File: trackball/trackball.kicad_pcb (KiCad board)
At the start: 2 copper layers, 15 x 13.4 mm, 8 parts, among them P8 CONN_7, U1 TLE4964-5M, U2 TLE4964-5M, U3 TLE4964-5M, U4 TLE4964-5M

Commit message: Bump version number to 1.2.0
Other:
- board text added: "v1.2.0"
- board text removed: "v1.1.0"
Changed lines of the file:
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@@
-(kicad_pcb (version 20171130) (host pcbnew "(5.1.5)-2")
+(kicad_pcb (version 20171130) (host pcbnew 5.1.5-52549c5~84~ubuntu18.04.1)
   (general
     (thickness 1.6)
@@
   (title_block
     (title "UHK Key Cluster Module - Trackball Board")
-    (rev 1.1.0)
+    (rev 1.2.0)
     (company "Ultimate Gadget Laboratories Kft.")
   )
@@
   )
   (setup
-    (last_trace_width 0.381)
+    (last_trace_width 0.2032)
     (user_trace_width 0.2032)
     (user_trace_width 0.254)
@@
   (gr_arc (start 205.382248 150.782505) (end 204.420921 150.506909) (angle -90) (layer Edge.Cuts) (width 0.01))
   (gr_arc (start 200.187782 143.931454) (end 200.937782 143.931454) (angle -180) (layer Edge.Cuts) (width 0.01))
-  (gr_text v1.1.0 (at 196.6 145 17) (layer B.SilkS)
+  (gr_text v1.2.0 (at 196.6 145 17) (layer B.SilkS)
     (effects (font (size 0.75 0.75) (thickness 0.15)) (justify mirror))
   )
@@
   (segment (start 198.5 149.1) (end 198.5 149.9) (width 0.254) (layer B.Cu) (net 1))
   (via (at 198.45 153.95) (size 0.7112) (drill 0.381) (layers F.Cu B.Cu) (net 1))
-  (segment (start 200.390425 147.2438) (end 200.335876 147.189251) (width 0.254) (layer F.Cu) (net 2))
-  (segment (start 200.085625 146.939) (end 200.335876 147.189251) (width 0.254) (layer F.Cu) (net 2))
-  (segment (start 199.9996 146.939) (end 200.085625 146.939) (width 0.254) (layer F.Cu) (net 2))
   (segment (start 203.4 155.03982) (end 203.58982 154.85) (width 0.254) (layer F.Cu) (net 1))
   (via (at 204.35 154.85) (size 0.7112) (drill 0.381) (layers F.Cu B.Cu) (net 1))
@@
   (via (at 198.6026 151.3078) (size 0.7112) (drill 0.381) (layers F.Cu B.Cu) (net 1))
   (segment (start 198.6026 150.2664) (end 197.485 149.1488) (width 0.508) (layer B.Cu) (net 1))
+  (segment (start 200.390425 147.2438) (end 200.335876 147.189251) (width 0.254) (layer F.Cu) (net 2))
+  (segment (start 200.085625 146.939) (end 200.335876 147.189251) (width 0.254) (layer F.Cu) (net 2))
+  (segment (start 199.9996 146.939) (end 200.085625 146.939) (width 0.254) (layer F.Cu) (net 2))
   (segment (start 199 146.999237) (end 199 149.1) (width 0.254) (layer B.Cu) (net 2))
   (via (at 199.009 147.193) (size 0.7112) (drill 0.381) (layers F.Cu B.Cu) (net 2))

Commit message: Bump the version number of both boards to 2.0.0
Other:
- board text added: "v2.0.0"
- board text removed: "v1.2.0"
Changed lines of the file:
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@@
   (title_block
     (title "UHK Key Cluster Module - Trackball Board")
-    (rev 1.2.0)
+    (rev 2.0.0)
     (company "Ultimate Gadget Laboratories Kft.")
   )
@@
   (gr_arc (start 205.382248 150.782505) (end 204.420921 150.506909) (angle -90) (layer Edge.Cuts) (width 0.01))
   (gr_arc (start 200.187782 143.931454) (end 200.937782 143.931454) (angle -180) (layer Edge.Cuts) (width 0.01))
-  (gr_text v1.2.0 (at 196.6 145 17) (layer B.SilkS)
+  (gr_text v2.0.0 (at 196.6 145 17) (layer B.SilkS)
     (effects (font (size 0.75 0.75) (thickness 0.15)) (justify mirror))
   )

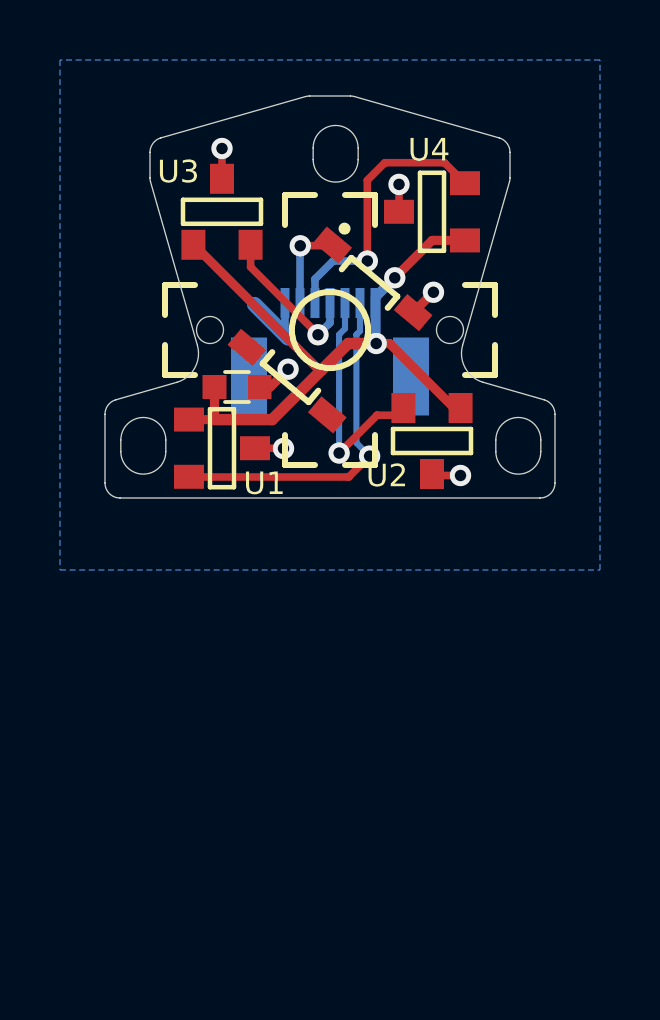
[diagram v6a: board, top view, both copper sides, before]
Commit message: Remove unneeded capacitor.
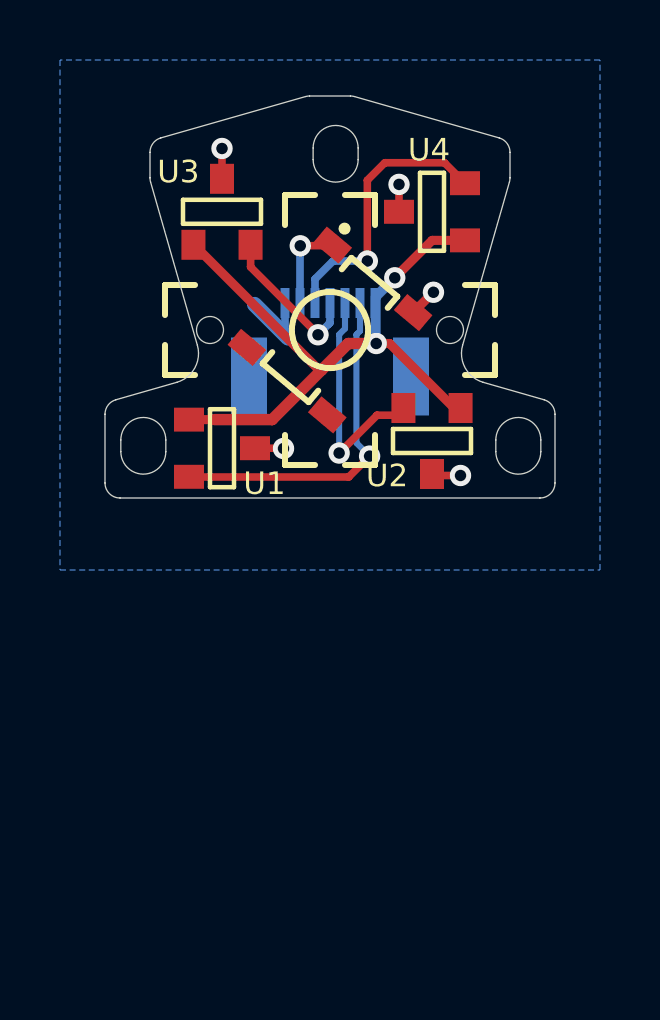
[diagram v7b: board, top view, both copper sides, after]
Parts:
- removed C1: 0.1uF, UGL:SM0603
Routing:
- net GND: track 8.44 -> 7.25 mm, vias 6 -> 5
- net +3V3: track 23.6 -> 22.5 mm
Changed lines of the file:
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@@
     (thickness 1.6)
     (drawings 41)
-    (tracks 75)
+    (tracks 71)
     (zones 0)
-    (modules 8)
+    (modules 7)
     (nets 8)
   )
@@
     (visible_elements 7FFFFF7F)
     (pcbplotparams
-      (layerselection 0x00030_ffffffff)
+      (layerselection 0x010fc_ffffffff)
       (usegerberextensions true)
       (usegerberattributes false)
@@
       (outputformat 1)
       (mirror false)
-      (drillshape 1)
+      (drillshape 0)
       (scaleselection 1)
       (outputdirectory ""))
@@
     (pad "" np_thru_hole circle (at 4 0) (size 0.9 0.9) (drill 0.9) (layers *.Cu *.Mask))
     (pad "" np_thru_hole circle (at -4 0) (size 0.9 0.9) (drill 0.9) (layers *.Cu *.Mask))
-  )
-  (module UGL:SM0603 (layer F.Cu)
-    (at 196.9 151.9 180)
-    (attr smd)
-    (fp_text reference C1 (at 1.5 -0.9 180) (layer B.SilkS)
-      (effects (font (size 0.75 0.75) (thickness 0.15)) (justify mirror))
-    )
-    (fp_text value 0.1uF (at 0.6 -2 180) (layer B.SilkS)
-      (effects (font (size 0.75 0.75) (thickness 0.15)) (justify mirror))
-    )
-    (fp_line (start -0.4 -0.5) (end 0.4 -0.5) (layer F.SilkS) (width 0.127))
-    (fp_line (start 0.4 0.5) (end -0.4 0.5) (layer F.SilkS) (width 0.127))
-    (pad 1 smd rect (at -0.75 0 180) (size 0.8 0.8) (layers F.Cu F.Paste F.Mask)
-      (net 1 GND))
-    (pad 2 smd rect (at 0.75 0 180) (size 0.8 0.8) (layers F.Cu F.Paste F.Mask)
-      (net 4 +3V3))
-    (model smd\resistors\R0603.wrl
-      (offset (xyz 0 0 0.02540000082496551))
-      (scale (xyz 0.5 0.5 0.5))
-      (rotate (xyz 0 0 0))
-    )
   )
   (module UGL:TL3315NF250Q (layer F.Cu)
@@
   (segment (start 202.770779 149.420429) (end 203.448808 148.7424) (width 0.3048) (layer F.Cu) (net 1))
   (via (at 203.448808 148.7424) (size 0.7112) (drill 0.381) (layers F.Cu B.Cu) (net 1))
-  (segment (start 198.0104 151.9) (end 198.6026 151.3078) (width 0.3048) (layer F.Cu) (net 1))
-  (segment (start 197.65 151.9) (end 198.0104 151.9) (width 0.3048) (layer F.Cu) (net 1))
-  (via (at 198.6026 151.3078) (size 0.7112) (drill 0.381) (layers F.Cu B.Cu) (net 1))
   (segment (start 198.6026 150.2664) (end 197.485 149.1488) (width 0.508) (layer B.Cu) (net 1))
   (segment (start 200.390425 147.2438) (end 200.335876 147.189251) (width 0.254) (layer F.Cu) (net 2))
@@
   (segment (start 201.9866 150.45) (end 201.541198 150.45) (width 0.3048) (layer F.Cu) (net 4))
   (segment (start 204.3525 152.8159) (end 201.9866 150.45) (width 0.3048) (layer F.Cu) (net 4))
-  (segment (start 196.15 152.9875) (end 196.15 151.9) (width 0.3048) (layer F.Cu) (net 4))
   (segment (start 195.30018 152.9875) (end 196.15 152.9875) (width 0.3048) (layer F.Cu) (net 4))
   (segment (start 200.608662 150.45) (end 201.541198 150.45) (width 0.381) (layer F.Cu) (net 4))

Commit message: Update contour to rigid-flex.
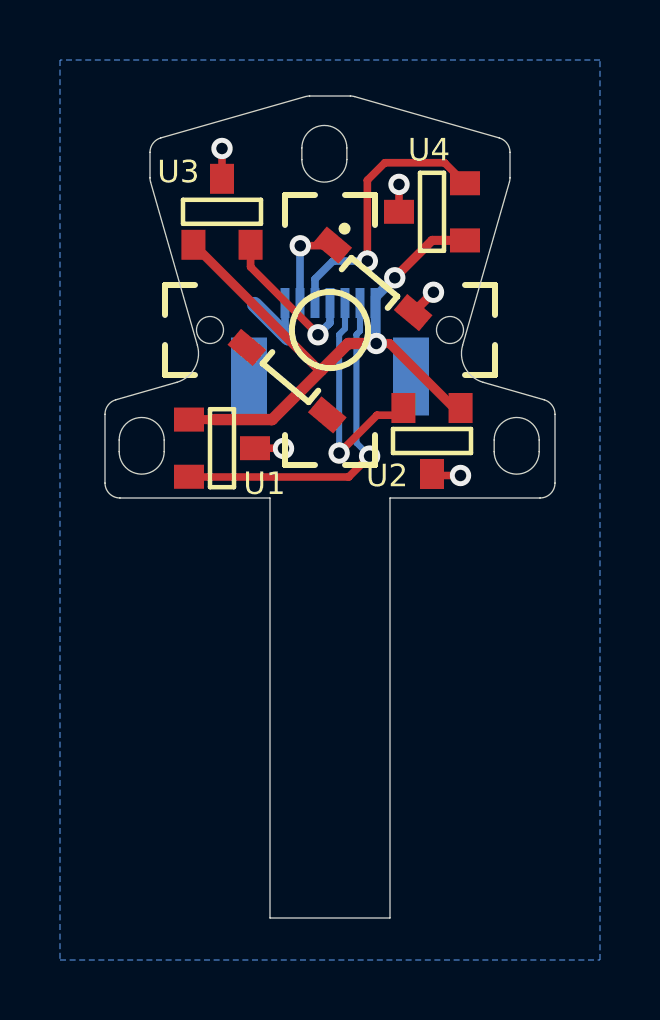
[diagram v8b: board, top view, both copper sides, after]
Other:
- board size 15 x 13.4 mm -> 15 x 27.4 mm
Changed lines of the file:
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@@
   (general
     (thickness 1.6)
-    (drawings 41)
+    (drawings 46)
     (tracks 71)
     (zones 0)
@@
     (37 F.SilkS user)
     (38 B.Mask user)
-    (39 F.Mask user)
+    (39 F.Mask user hide)
     (40 Dwgs.User user)
     (41 Cmts.User user)
@@
     (pad_to_mask_clearance 0)
     (aux_axis_origin 0 0)
-    (visible_elements 7FFFFF7F)
+    (visible_elements 7FFFEF7F)
     (pcbplotparams
       (layerselection 0x010fc_ffffffff)
@@
     (pad 4 smd rect (at -2.225 -1.749999 230) (size 0.7 1.1) (layers F.Cu F.Paste F.Mask))
   )
+  (gr_line (start 202 155.6) (end 207 155.6) (angle 90) (layer Edge.Cuts) (width 0.01))
   (gr_circle (center 196.3 153.94) (end 196.35 153.94) (layer Eco2.User) (width 0.1))
   (gr_circle (center 203.94 146.06) (end 203.99 146.06) (layer Eco2.User) (width 0.1))
   (gr_circle (center 203.94 153.94) (end 203.99 153.94) (layer Eco2.User) (width 0.1))
   (gr_circle (center 196.06 146.06) (end 196.11 146.06) (layer Eco2.User) (width 0.1))
-  (gr_arc (start 199.320057 142.700091) (end 199.32003 142.199997) (angle -15.6) (layer Edge.Cuts) (width 0.01))
-  (gr_arc (start 200.679943 142.700091) (end 200.817329 142.219238) (angle -15.7) (layer Edge.Cuts) (width 0.01))
-  (gr_arc (start 193.000061 155.099935) (end 192.5 155.100003) (angle -89.9) (layer Edge.Cuts) (width 0.01))
-  (gr_arc (start 194.500041 144.077192) (end 194.36264 143.59639) (angle -74) (layer Edge.Cuts) (width 0.01))
-  (gr_arc (start 205.499959 144.077192) (end 206 144.077148) (angle -74) (layer Edge.Cuts) (width 0.01))
-  (gr_arc (start 206.999958 152.806915) (end 207.5 152.806897) (angle -74) (layer Edge.Cuts) (width 0.01))
-  (gr_arc (start 206.999932 155.099935) (end 207 155.600003) (angle -89.9) (layer Edge.Cuts) (width 0.01))
-  (gr_arc (start 193.000042 152.806915) (end 192.862183 152.32626) (angle -74) (layer Edge.Cuts) (width 0.01))
-  (gr_arc (start 194.5001 144.929701) (end 194 144.92973) (angle -15.97224935) (layer Edge.Cuts) (width 0.01))
-  (gr_arc (start 205.4999 144.929701) (end 205.980629 145.067548) (angle -16) (layer Edge.Cuts) (width 0.01))
-  (gr_line (start 207 155.600003) (end 193 155.600003) (angle 90) (layer Edge.Cuts) (width 0.01))
-  (gr_line (start 207.5 152.806897) (end 207.5 155.100003) (angle 90) (layer Edge.Cuts) (width 0.01))
-  (gr_line (start 192.862183 152.32626) (end 194.893456 151.743802) (angle 90) (layer Edge.Cuts) (width 0.01))
-  (gr_line (start 195.579079 150.506909) (end 194.019371 145.067548) (angle 90) (layer Edge.Cuts) (width 0.01))
-  (gr_line (start 200.817329 142.219238) (end 205.63736 143.59639) (angle 90) (layer Edge.Cuts) (width 0.01))
-  (gr_line (start 194.36264 143.59639) (end 199.182671 142.219238) (angle 90) (layer Edge.Cuts) (width 0.01))
-  (gr_line (start 194 144.92973) (end 194 144.077148) (angle 90) (layer Edge.Cuts) (width 0.01))
-  (gr_line (start 205.106544 151.743802) (end 207.137817 152.32626) (angle 90) (layer Edge.Cuts) (width 0.01))
-  (gr_line (start 199.32003 142.199997) (end 200.67997 142.199997) (angle 90) (layer Edge.Cuts) (width 0.01))
-  (gr_line (start 206 144.077148) (end 206 144.92973) (angle 90) (layer Edge.Cuts) (width 0.01))
-  (gr_line (start 205.980629 145.067548) (end 204.420921 150.506909) (angle 90) (layer Edge.Cuts) (width 0.01))
-  (gr_line (start 205.52729 154.054501) (end 205.52729 153.665707) (angle 90) (layer Edge.Cuts) (width 0.01))
-  (gr_arc (start 200.187782 144.320233) (end 199.437782 144.320233) (angle -180) (layer Edge.Cuts) (width 0.01))
-  (gr_arc (start 193.77729 153.665707) (end 194.52729 153.665707) (angle -180) (layer Edge.Cuts) (width 0.01))
-  (gr_line (start 192.5 155.100003) (end 192.5 152.806897) (angle 90) (layer Edge.Cuts) (width 0.01))
-  (gr_line (start 194.52729 153.665707) (end 194.52729 154.054501) (angle 90) (layer Edge.Cuts) (width 0.01))
-  (gr_arc (start 206.27729 153.665707) (end 207.02729 153.665707) (angle -180) (layer Edge.Cuts) (width 0.01))
-  (gr_line (start 193.02729 154.054501) (end 193.02729 153.665707) (angle 90) (layer Edge.Cuts) (width 0.01))
-  (gr_line (start 207.02729 153.665707) (end 207.02729 154.054501) (angle 90) (layer Edge.Cuts) (width 0.01))
-  (gr_arc (start 194.617759 150.782505) (end 194.893456 151.743802) (angle -90) (layer Edge.Cuts) (width 0.01))
-  (gr_line (start 200.937782 143.931454) (end 200.937782 144.320233) (angle 90) (layer Edge.Cuts) (width 0.01))
-  (gr_line (start 199.437782 144.320233) (end 199.437782 143.931454) (angle 90) (layer Edge.Cuts) (width 0.01))
-  (gr_arc (start 206.27729 154.054501) (end 205.52729 154.054501) (angle -180) (layer Edge.Cuts) (width 0.01))
-  (gr_arc (start 193.77729 154.054501) (end 193.02729 154.054501) (angle -180) (layer Edge.Cuts) (width 0.01))
-  (gr_arc (start 205.382248 150.782505) (end 204.420921 150.506909) (angle -90) (layer Edge.Cuts) (width 0.01))
-  (gr_arc (start 200.187782 143.931454) (end 200.937782 143.931454) (angle -180) (layer Edge.Cuts) (width 0.01))
   (gr_text v2.0.0 (at 196.6 145 17) (layer B.SilkS)
     (effects (font (size 0.75 0.75) (thickness 0.15)) (justify mirror))
   )
+  (gr_arc (start 205.499996 144.077151) (end 206 144.077151) (angle -74.05780781) (layer Edge.Cuts) (width 0.01))
+  (gr_arc (start 200.67997 142.700007) (end 200.817333 142.219238) (angle -15.97405795) (layer Edge.Cuts) (width 0.01))
+  (gr_arc (start 199.320037 142.700022) (end 199.320027 142.2) (angle -15.55315467) (layer Edge.Cuts) (width 0.01))
+  (gr_arc (start 194.500004 144.077151) (end 194.362639 143.596389) (angle -74.04666612) (layer Edge.Cuts) (width 0.01))
+  (gr_arc (start 194.500002 144.929718) (end 194 144.92973) (angle -16.28978266) (layer Edge.Cuts) (width 0.01))
+  (gr_arc (start 193.000003 152.806895) (end 192.862181 152.326264) (angle -73.99483282) (layer Edge.Cuts) (width 0.01))
+  (gr_arc (start 192.999992 155.100005) (end 192.5 155.1) (angle -90.00219193) (layer Edge.Cuts) (width 0.01))
+  (gr_arc (start 207.000008 155.100005) (end 207 155.6) (angle -90.00795646) (layer Edge.Cuts) (width 0.01))
+  (gr_arc (start 206.999997 152.806895) (end 207.5 152.806895) (angle -74.00205761) (layer Edge.Cuts) (width 0.01))
+  (gr_arc (start 205.499998 144.929718) (end 205.980631 145.067548) (angle -16.5242857) (layer Edge.Cuts) (width 0.01))
+  (gr_arc (start 206.222717 153.665717) (end 206.97271 153.66571) (angle -179.9978282) (layer Edge.Cuts) (width 0.01))
+  (gr_line (start 206.97271 153.66571) (end 206.97271 154.054501) (angle 90) (layer Edge.Cuts) (width 0.01))
+  (gr_arc (start 206.222725 154.05448) (end 205.47271 154.054501) (angle -179.9990721) (layer Edge.Cuts) (width 0.01))
+  (gr_line (start 205.47271 154.054501) (end 205.47271 153.66571) (angle 90) (layer Edge.Cuts) (width 0.01))
+  (gr_arc (start 193.72271 153.665717) (end 194.47271 153.66571) (angle -179.9989939) (layer Edge.Cuts) (width 0.01))
+  (gr_line (start 194.47271 153.66571) (end 194.47271 154.054501) (angle 90) (layer Edge.Cuts) (width 0.01))
+  (gr_arc (start 193.722717 154.05448) (end 192.97271 154.054501) (angle -179.9979064) (layer Edge.Cuts) (width 0.01))
+  (gr_line (start 192.97271 154.054501) (end 192.97271 153.66571) (angle 90) (layer Edge.Cuts) (width 0.01))
+  (gr_arc (start 199.812233 144.320227) (end 199.062217 144.320239) (angle -180.0005206) (layer Edge.Cuts) (width 0.01))
+  (gr_line (start 199.062217 144.320239) (end 199.062217 143.931448) (angle 90) (layer Edge.Cuts) (width 0.01))
+  (gr_arc (start 199.812225 143.931448) (end 200.562217 143.931448) (angle -179.9987111) (layer Edge.Cuts) (width 0.01))
+  (gr_line (start 200.562217 143.931448) (end 200.562217 144.320239) (angle 90) (layer Edge.Cuts) (width 0.01))
+  (gr_line (start 200.817333 142.219238) (end 205.637361 143.596389) (angle 90) (layer Edge.Cuts) (width 0.01))
+  (gr_line (start 199.320027 142.2) (end 200.679973 142.2) (angle 90) (layer Edge.Cuts) (width 0.01))
+  (gr_line (start 194.362639 143.596389) (end 199.182667 142.219238) (angle 90) (layer Edge.Cuts) (width 0.01))
+  (gr_line (start 194 144.92973) (end 194 144.077151) (angle 90) (layer Edge.Cuts) (width 0.01))
+  (gr_line (start 194.019369 145.067548) (end 195.57908 150.506907) (angle 90) (layer Edge.Cuts) (width 0.01))
+  (gr_line (start 194.893456 151.743806) (end 192.862181 152.326264) (angle 90) (layer Edge.Cuts) (width 0.01))
+  (gr_line (start 192.5 152.806895) (end 192.5 155.1) (angle 90) (layer Edge.Cuts) (width 0.01))
+  (gr_line (start 193 155.6) (end 198 155.6) (angle 90) (layer Edge.Cuts) (width 0.01))
+  (gr_line (start 207.5 155.1) (end 207.5 152.806895) (angle 90) (layer Edge.Cuts) (width 0.01))
+  (gr_line (start 207.137819 152.326264) (end 205.106544 151.743806) (angle 90) (layer Edge.Cuts) (width 0.01))
+  (gr_line (start 204.42092 150.506907) (end 205.980631 145.067548) (angle 90) (layer Edge.Cuts) (width 0.01))
+  (gr_line (start 206 144.92973) (end 206 144.077151) (angle 90) (layer Edge.Cuts) (width 0.01))
+  (gr_arc (start 194.617835 150.782546) (end 194.893456 151.743806) (angle -90.00852698) (layer Edge.Cuts) (width 0.01))
+  (gr_arc (start 205.382173 150.782546) (end 204.42092 150.506907) (angle -90.00052091) (layer Edge.Cuts) (width 0.01))
+  (gr_line (start 198 155.6) (end 198 169.6) (angle 90) (layer Edge.Cuts) (width 0.01))
+  (gr_line (start 202 155.6) (end 202 169.6) (angle 90) (layer Edge.Cuts) (width 0.01))
+  (gr_line (start 202 169.6) (end 198 169.6) (angle 90) (layer Edge.Cuts) (width 0.01))
+  (gr_line (start 198 164.6) (end 202 164.6) (angle 90) (layer Margin) (width 0.01))
   (via (at 196.4 143.95) (size 0.7112) (drill 0.381) (layers F.Cu B.Cu) (net 1))
   (segment (start 198.5 149.1) (end 198.5 149.9) (width 0.254) (layer B.Cu) (net 1))
@@
     (polygon
       (pts
-        (xy 191 158) (xy 209 158) (xy 209 141) (xy 191 141)
+        (xy 191 171) (xy 209 171) (xy 209 141) (xy 191 141)
       )
     )
